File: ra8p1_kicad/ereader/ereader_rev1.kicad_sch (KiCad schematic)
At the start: 0 parts

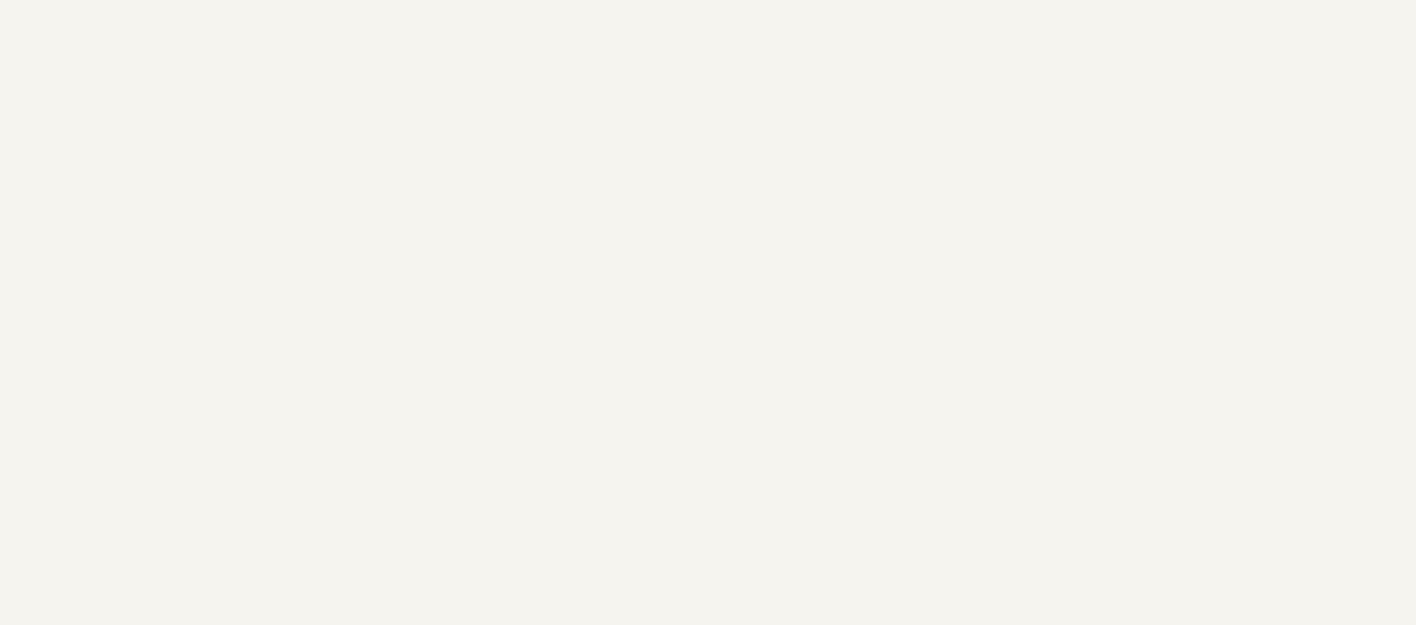
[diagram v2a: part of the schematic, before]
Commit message: Add ESP32-C6 radio sheet with sourced bypass network and calculations
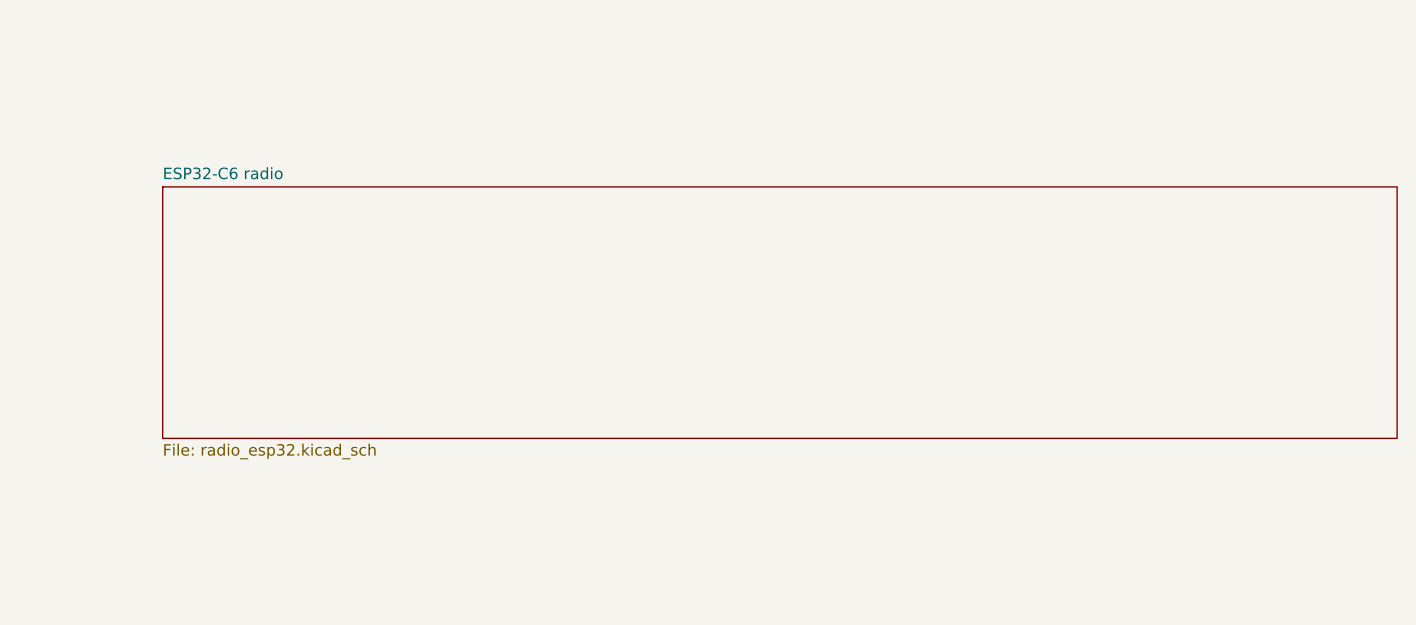
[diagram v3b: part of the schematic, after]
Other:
- added sheet ESP32-C6 radio (radio_esp32.kicad_sch)
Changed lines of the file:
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@@
+	)
+	(sheet
+		(at 203.2 129.54)
+		(size 137.16 27.94)
+		(exclude_from_sim no)
+		(in_bom yes)
+		(on_board yes)
+		(dnp no)
+		(fields_autoplaced yes)
+		(stroke
+			(width 0.1524)
+			(type solid)
+		)
+		(fill
+			(color 0 0 0 0)
+		)
+		(property "Sheetname" "ESP32-C6 radio"
+			(at 203.2 128.8284 0)
+			(show_name no)
+			(do_not_autoplace no)
+			(effects
+				(font
+					(size 1.27 1.27)
+				)
+				(justify left bottom)
+			)
+		)
+		(property "Sheetfile" "radio_esp32.kicad_sch"
+			(at 203.2 158.0646 0)
+			(show_name no)
+			(do_not_autoplace no)
+			(effects
+				(font
+					(size 1.27 1.27)
+				)
+				(justify left top)
+			)
+		)
+		(instances
+			(project "ereader_rev1"
+				(path "/0586cc51-9c57-495b-a0c9-c29ba0d48166"
+					(page "6")
+				)
+			)
+		)
 	)
 	(sheet

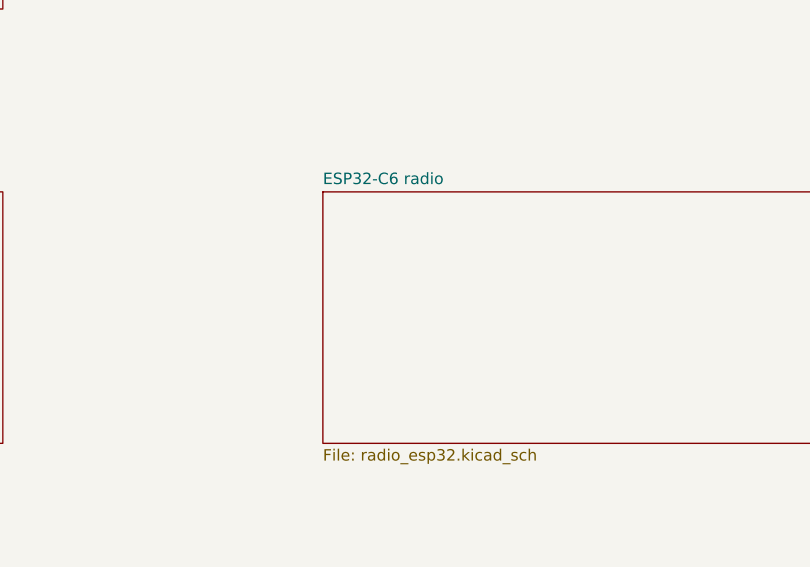
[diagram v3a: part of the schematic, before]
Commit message: Add radio enable divider with verified logic-level screening
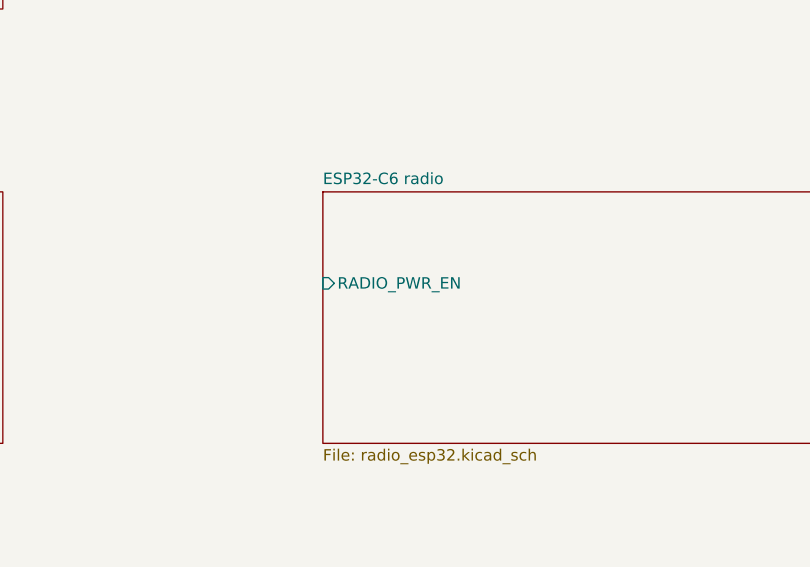
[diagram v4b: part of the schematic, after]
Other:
- sheet ESP32-C6 radio ports: added RADIO_PWR_EN; removed none
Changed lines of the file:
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@@
+			)
+		)
+		(pin "RADIO_PWR_EN" input
+			(at 203.2 139.7 180)
+			(effects
+				(font
+					(size 1.27 1.27)
+				)
+				(justify left)
 			)
 		)

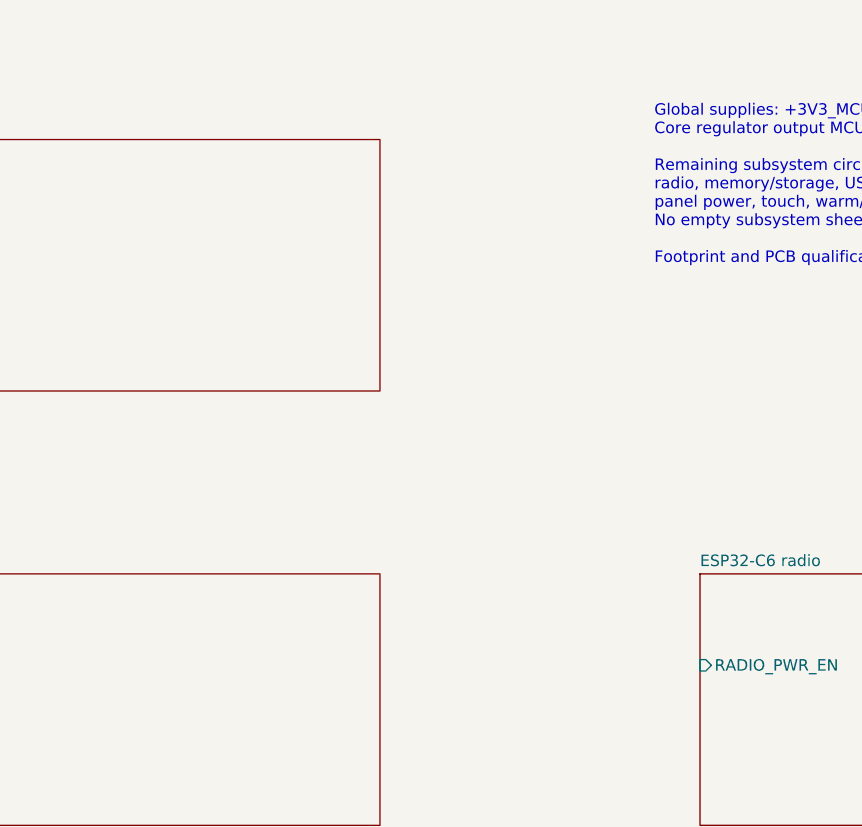
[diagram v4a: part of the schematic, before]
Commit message: Allocate RA8P1 SPI radio interface and connect power enable
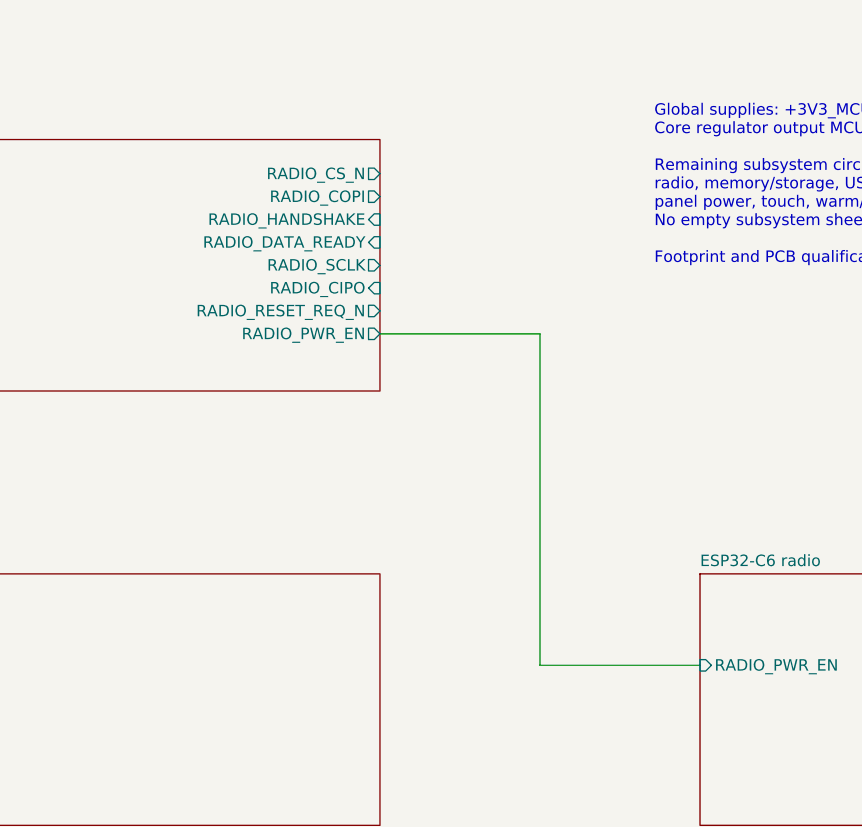
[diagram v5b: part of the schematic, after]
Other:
- sheet RA8P1 IO allocation ports: added RADIO_CIPO, RADIO_COPI, RADIO_CS_N, RADIO_DATA_READY, RADIO_HANDSHAKE, RADIO_PWR_EN, RADIO_RESET_REQ_N, RADIO_SCLK; removed none
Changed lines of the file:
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@@
+		)
+	)
+	(wire
+		(pts
+			(xy 185.42 102.87) (xy 185.42 139.7)
+		)
+		(stroke
+			(width 0)
+			(type default)
+		)
+	)
+	(wire
+		(pts
+			(xy 167.64 102.87) (xy 185.42 102.87)
+		)
+		(stroke
+			(width 0)
+			(type default)
+		)
+	)
+	(wire
+		(pts
+			(xy 185.42 139.7) (xy 203.2 139.7)
+		)
+		(stroke
+			(width 0)
+			(type default)
 		)
 	)
@@
 			)
 		)
+		(pin "RADIO_CS_N" output
+			(at 167.64 85.09 0)
+			(effects
+				(font
+					(size 1.27 1.27)
+				)
+				(justify right)
+			)
+		)
+		(pin "RADIO_COPI" output
+			(at 167.64 87.63 0)
+			(effects
+				(font
+					(size 1.27 1.27)
+				)
+				(justify right)
+			)
+		)
+		(pin "RADIO_HANDSHAKE" input
+			(at 167.64 90.17 0)
+			(effects
+				(font
+					(size 1.27 1.27)
+				)
+				(justify right)
+			)
+		)
+		(pin "RADIO_DATA_READY" input
+			(at 167.64 92.71 0)
+			(effects
+				(font
+					(size 1.27 1.27)
+				)
+				(justify right)
+			)
+		)
+		(pin "RADIO_SCLK" output
+			(at 167.64 95.25 0)
+			(effects
+				(font
+					(size 1.27 1.27)
+				)
+				(justify right)
+			)
+		)
+		(pin "RADIO_CIPO" input
+			(at 167.64 97.79 0)
+			(effects
+				(font
+					(size 1.27 1.27)
+				)
+				(justify right)
+			)
+		)
+		(pin "RADIO_RESET_REQ_N" output
+			(at 167.64 100.33 0)
+			(effects
+				(font
+					(size 1.27 1.27)
+				)
+				(justify right)
+			)
+		)
+		(pin "RADIO_PWR_EN" output
+			(at 167.64 102.87 0)
+			(effects
+				(font
+					(size 1.27 1.27)
+				)
+				(justify right)
+			)
+		)

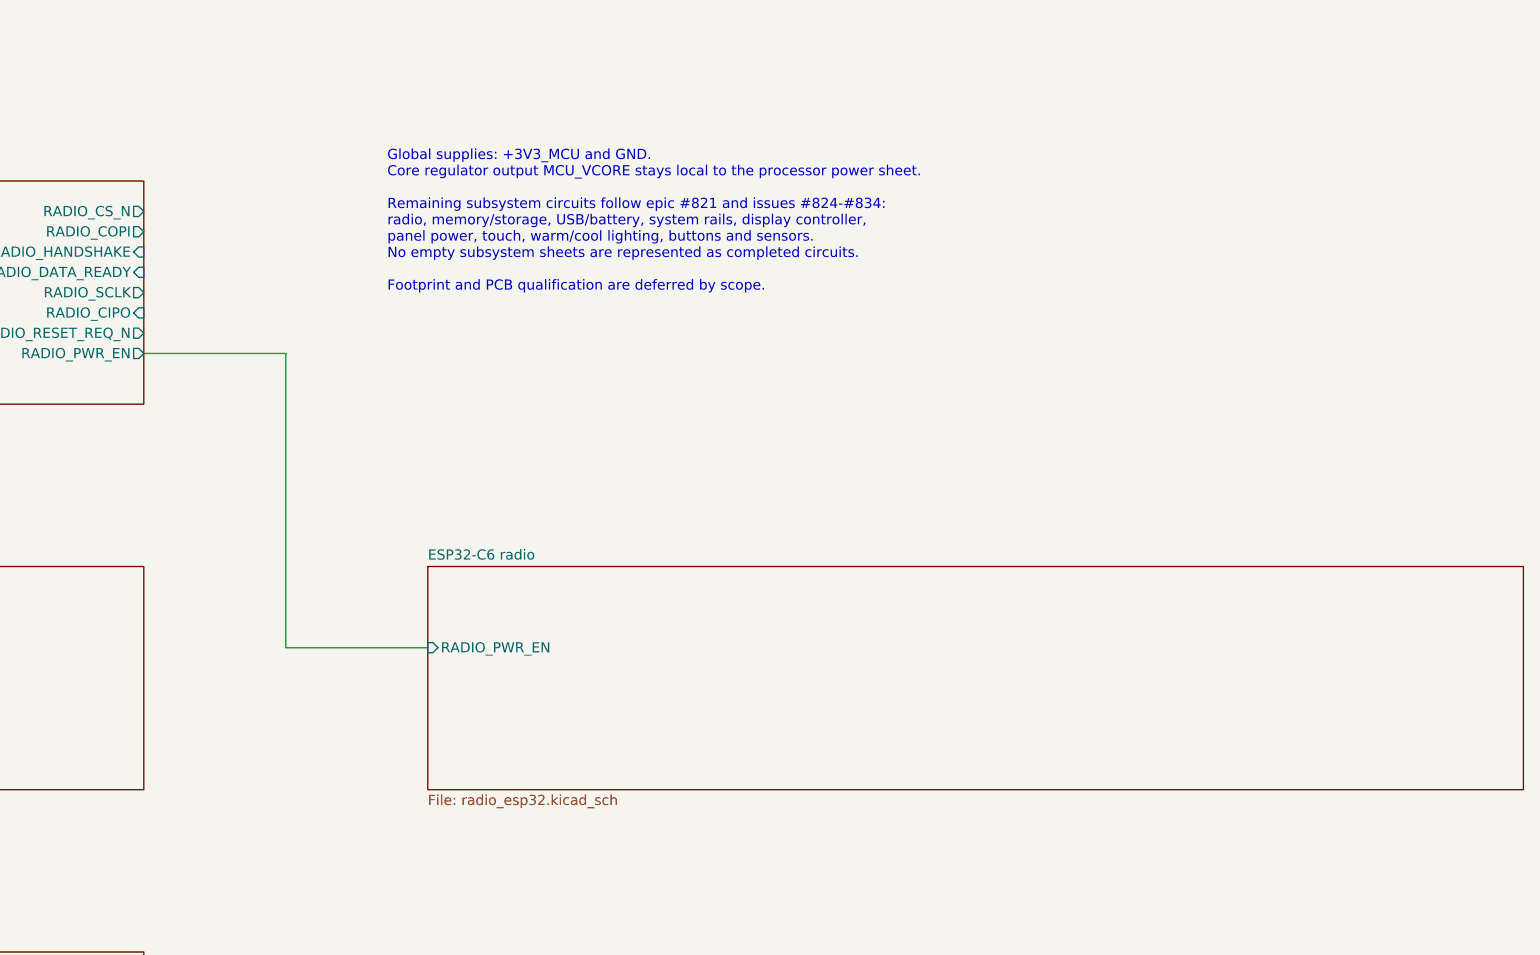
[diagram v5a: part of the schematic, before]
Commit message: Connect RA8P1 host SPI through the radio hierarchy
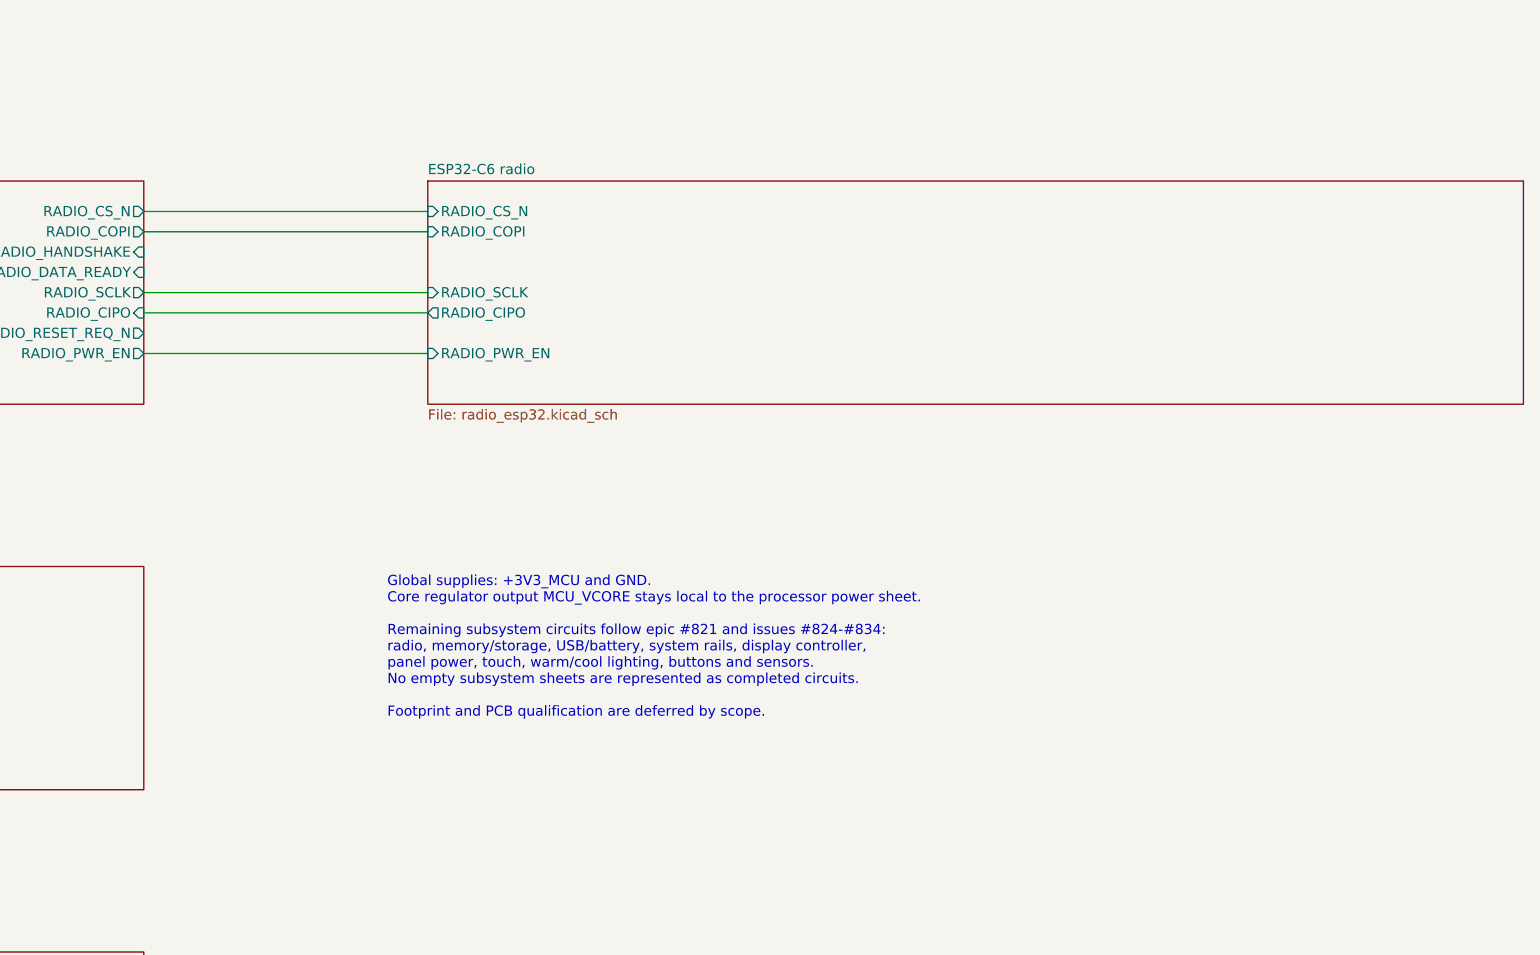
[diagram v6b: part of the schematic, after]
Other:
- sheet ESP32-C6 radio ports: added RADIO_CIPO, RADIO_COPI, RADIO_CS_N, RADIO_SCLK; removed none
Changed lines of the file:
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@@
 	(text "Global supplies: +3V3_MCU and GND.\nCore regulator output MCU_VCORE stays local to the processor power sheet.\n\nRemaining subsystem circuits follow epic #821 and issues #824-#834:\nradio, memory/storage, USB/battery, system rails, display controller,\npanel power, touch, warm/cool lighting, buttons and sensors.\nNo empty subsystem sheets are represented as completed circuits.\n\nFootprint and PCB qualification are deferred by scope."
 		(exclude_from_sim no)
-		(at 198.12 86.36 0)
+		(at 198.12 139.7 0)
 		(effects
 			(font
@@
 	(wire
 		(pts
-			(xy 185.42 102.87) (xy 185.42 139.7)
-		)
-		(stroke
-			(width 0)
-			(type default)
-		)
-	)
-	(wire
-		(pts
-			(xy 167.64 102.87) (xy 185.42 102.87)
-		)
-		(stroke
-			(width 0)
-			(type default)
-		)
-	)
-	(wire
-		(pts
-			(xy 185.42 139.7) (xy 203.2 139.7)
+			(xy 167.64 97.79) (xy 203.2 97.79)
+		)
+		(stroke
+			(width 0)
+			(type default)
+		)
+	)
+	(wire
+		(pts
+			(xy 167.64 102.87) (xy 203.2 102.87)
+		)
+		(stroke
+			(width 0)
+			(type default)
+		)
+	)
+	(wire
+		(pts
+			(xy 167.64 95.25) (xy 203.2 95.25)
+		)
+		(stroke
+			(width 0)
+			(type default)
+		)
+	)
+	(wire
+		(pts
+			(xy 167.64 85.09) (xy 203.2 85.09)
+		)
+		(stroke
+			(width 0)
+			(type default)
+		)
+	)
+	(wire
+		(pts
+			(xy 167.64 87.63) (xy 203.2 87.63)
 		)
 		(stroke
@@
 	)
 	(sheet
-		(at 203.2 129.54)
+		(at 203.2 81.28)
 		(size 137.16 27.94)
 		(exclude_from_sim no)
@@
 		)
 		(property "Sheetname" "ESP32-C6 radio"
-			(at 203.2 128.8284 0)
+			(at 203.2 80.5684 0)
 			(show_name no)
 			(do_not_autoplace no)
@@
 		)
 		(property "Sheetfile" "radio_esp32.kicad_sch"
-			(at 203.2 158.0646 0)
+			(at 203.2 109.8046 0)
 			(show_name no)
 			(do_not_autoplace no)
@@
 		)
 		(pin "RADIO_PWR_EN" input
-			(at 203.2 139.7 180)
-			(effects
-				(font
+			(at 203.2 102.87 180)
+			(effects
+				(font
+					(size 1.27 1.27)
+				)
+				(justify left)
+			)
+		)
+		(pin "RADIO_CIPO" output
+			(at 203.2 97.79 180)
+			(effects
+				(font
+					(size 1.27 1.27)
+				)
+				(justify left)
+			)
+		)
+		(pin "RADIO_COPI" input
+			(at 203.2 87.63 180)
+			(effects
+				(font
+					(size 1.27 1.27)
+				)
+				(justify left)
+			)
+		)
+		(pin "RADIO_CS_N" input
+			(at 203.2 85.09 180)
+			(effects
+				(font
+					(size 1.27 1.27)
+				)
+				(justify left)
+			)
+		)
+		(pin "RADIO_SCLK" input
+			(at 203.2 95.25 180)
+			(effects
+				(font

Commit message: Connect radio reset controls through schematic hierarchy
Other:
- sheet ESP32-C6 radio ports: added MCU_RESET_N, RADIO_RESET_REQ_N; removed none
- sheet RA8P1 clocks, reset and debug ports: added MCU_RESET_N; removed none
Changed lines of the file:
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@@
+	(wire
+		(pts
+			(xy 167.64 240.03) (xy 177.8 240.03)
+		)
+		(stroke
+			(width 0)
+			(type default)
+		)
+	)
+	(wire
+		(pts
+			(xy 193.04 105.41) (xy 203.2 105.41)
+		)
+		(stroke
+			(width 0)
+			(type default)
+		)
+	)
 	(wire
 		(pts
@@
 	(wire
 		(pts
+			(xy 167.64 100.33) (xy 203.2 100.33)
+		)
+		(stroke
+			(width 0)
+			(type default)
+		)
+	)
+	(wire
+		(pts
 			(xy 167.64 85.09) (xy 203.2 85.09)
 		)
@@
 			(width 0)
 			(type default)
+		)
+	)
+	(label "MCU_RESET_N"
+		(at 177.8 240.03 0)
+		(effects
+			(font
+				(size 1.27 1.27)
+			)
+			(justify left bottom)
+		)
+	)
+	(label "MCU_RESET_N"
+		(at 193.04 105.41 180)
+		(effects
+			(font
+				(size 1.27 1.27)
+			)
+			(justify right bottom)
 		)
 	)
@@
 				)
 				(justify left)
+			)
+		)
+		(pin "MCU_RESET_N" output
+			(at 167.64 240.03 0)
+			(effects
+				(font
+					(size 1.27 1.27)
+				)
+				(justify right)
 			)
 		)
@@
 			(effects
 				(font
+					(size 1.27 1.27)
+				)
+				(justify left)
+			)
+		)
+		(pin "RADIO_RESET_REQ_N" input
+			(at 203.2 100.33 180)
+			(effects
+				(font
+					(size 1.27 1.27)
+				)
+				(justify left)
+			)
+		)
+		(pin "MCU_RESET_N" input
+			(at 203.2 105.41 180)
+			(effects
+				(font
